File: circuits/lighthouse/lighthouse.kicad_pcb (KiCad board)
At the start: 2 copper layers, 84 x 112 mm, 83 parts, among them IC1 SX1308, J1 USB_C_Receptacle_PowerOnly_6P, J2 USB_B_Micro, Q1 S9013, Q2 FS8205A, Q3 2N7002K, Q4 SS8050, Q5 SS8050, U1 R300, U10 CP2102-GMR, U2 AMS1117-3.3, U4 TP4056-42-ESOP8, U5 DW01A, U6 AMS1117-3.3, U7 ESP32-WROOM-32

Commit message: Rewamped the pcb
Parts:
- removed J2: USB_B_Micro, Connector_USB:USB_Micro-B_Amphenol_10103594-0001LF_Horizontal
- removed R8: 2, Resistor_SMD:R_1206_3216Metric_Pad1.30x1.75mm_HandSolder
- BZ1: footprint Buzzer_Beeper:Buzzer_12x9.5RM7.6 -> Buzzer_Beeper:MagneticBuzzer_PUI_AT-0927-TT-6-R
- C4, C5: value C -> 10u
- J1: value USB_C_Receptacle_PowerOnly_6P -> USB_C_Receptacle_6P
- moved R4 28.4 mm to (91.4, 105.8)
- moved D12 25.6 mm to (82.7, 118.0)
- moved C6 21.4 mm to (112.3, 103.5)
- moved C7 21.4 mm to (112.3, 106.0)
- moved C12 21.3 mm to (88.0, 117.4), turned to -90 degrees
- moved Q1 20.9 mm to (97.0, 105.7)
- moved D8 20.9 mm to (104.3, 104.0), turned to -90 degrees
- moved R7 20.7 mm to (91.5, 103.0), turned to 180 degrees
- moved C13 20.5 mm to (88.0, 110.4), turned to 90 degrees
- moved R5 19.9 mm to (49.5, 110.0)
- moved BZ1 19.9 mm to (95.0, 118.0)
- moved R32 19.4 mm to (49.5, 94.8), turned to 90 degrees
- moved R16 19.3 mm to (107.3, 104.0), turned to 90 degrees
- moved D11 18.8 mm to (113.7, 114.9)
- moved R19 18.8 mm to (111.2, 114.9)
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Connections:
- net Net-(U7-IO22) renamed RFID_PW_SENSE
- C3 pad 1: Net-(U4-CE) -> +5V
- D5 pad 2: Net-(D5-A) -> +5V
- D6 pad 2: Net-(D5-A) -> +5V
- J1 pad A5: Net-(J1-CC1) -> /Charger/D+
- J1 pad A9: Net-(U4-CE) -> +5V
- J1 pad B5: Net-(J1-CC2) -> /Charger/D-
- J1 pad B9: Net-(U4-CE) -> +5V
- R32 pad 1: Net-(J1-CC2) -> /Charger/D-
- R33 pad 1: Net-(J1-CC1) -> /Charger/D+
- U10 pad 4: Net-(J2-D+) -> /Charger/D+
- U10 pad 5: Net-(J2-D-) -> /Charger/D-
- U4 pad 4: Net-(U4-CE) -> +5V
- U4 pad 8: Net-(U4-CE) -> +5V
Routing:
- net GND: track 167.3 -> 110.8 mm, vias 10 -> 14
- net Net-(U4-CE): track 42.8 -> 0.00 mm, vias 2 -> 0
- net +5V: track 119.8 -> 162.3 mm, vias 2 -> 4
- net RFID_PW: track 11.7 -> 44.1 mm
- net RFID_PW_SENSE: track 27.1 -> 46.7 mm
- net ESP25: track 53.1 -> 34.6 mm, vias 2 -> 4
- net /Charger/+BAT: track 90.7 -> 72.6 mm
- net +3.3V: track 127.7 -> 109.9 mm
- net EN: track 28.2 -> 11.0 mm
- net /Charger/-BAT: track 67.4 -> 81.5 mm
- net Net-(Q1-B): track 18.1 -> 4.57 mm
- net /Charger/D+: track 0.00 -> 11.9 mm
- net /Charger/D-: track 0.00 -> 11.0 mm
- net Net-(D5-A): track 10.2 -> 0.00 mm
- net Net-(U1-EN): track 13.1 -> 3.43 mm
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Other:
- board size 84 x 112 mm -> 83 x 80 mm

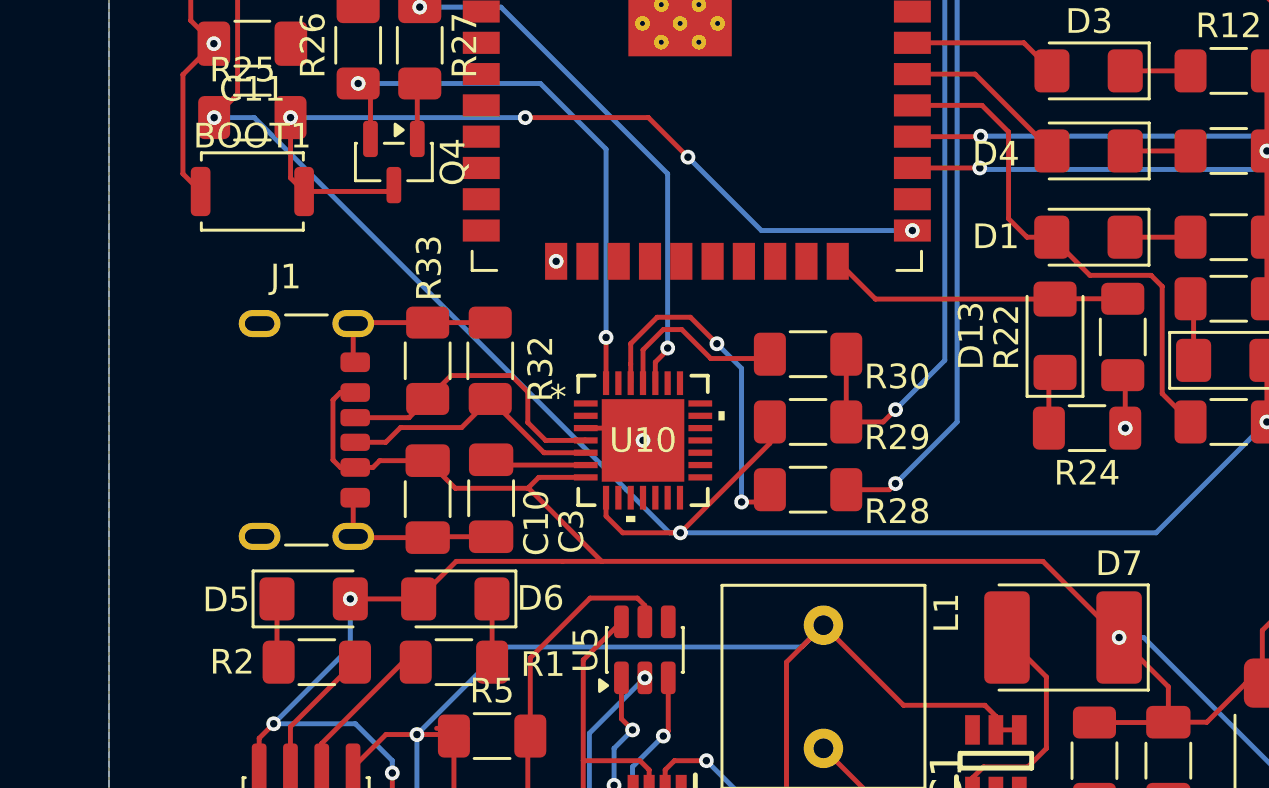
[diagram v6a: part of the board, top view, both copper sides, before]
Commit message: Changed to a correct usb C port
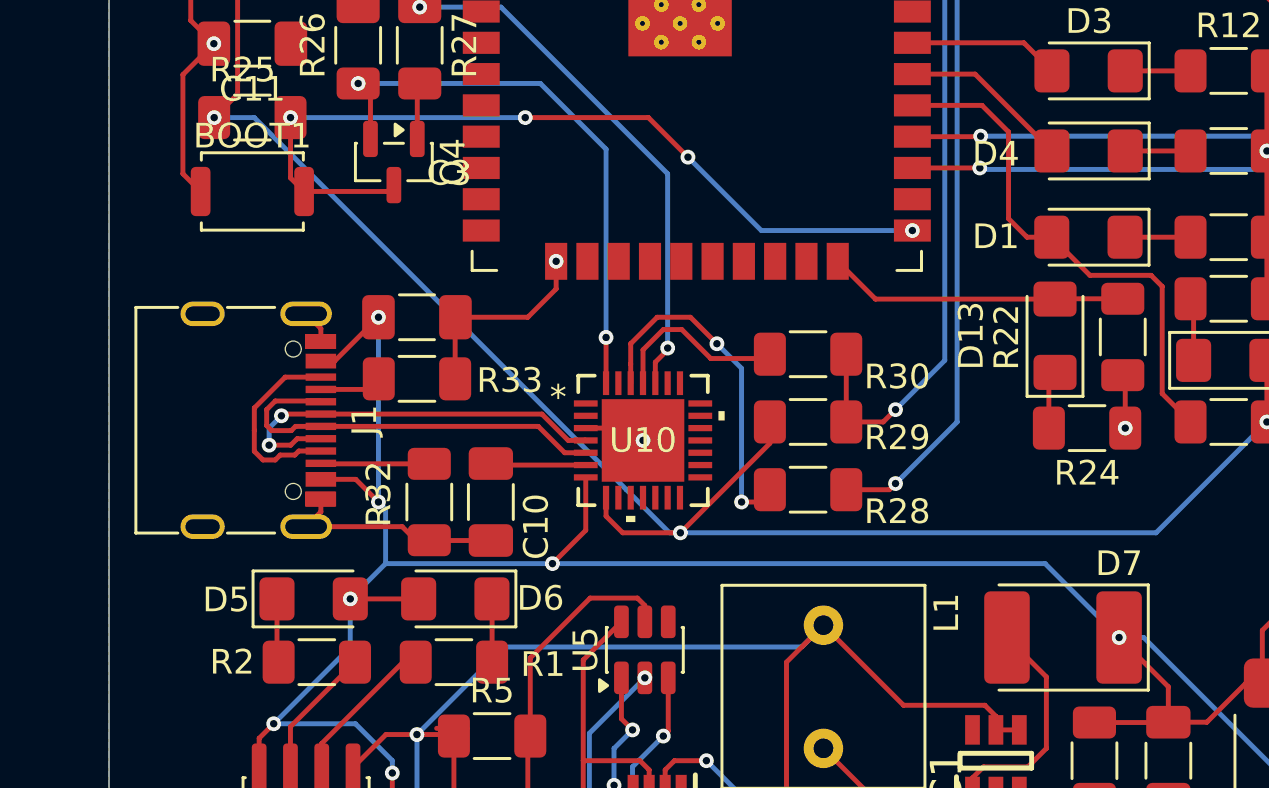
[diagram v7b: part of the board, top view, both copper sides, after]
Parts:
- J1: value USB_C_Receptacle_6P -> USB_C_Receptacle_USB2.0_14P; footprint Connector_USB:USB_C_Receptacle_GCT_USB4125-xx-x_6P_TopMnt_Horizontal -> Connector_USB:USB_C_Receptacle_G-Switch_GT-USB-7010ASV
- moved C3 7.40 mm to (46.5, 93.0), turned to 0 degrees
- moved R32 6.24 mm to (47.0, 100.5), turned to -90 degrees
- moved J1 2.08 mm to (38.9, 97.2)
- moved R33 0.85 mm to (46.5, 95.5), turned to 0 degrees
- moved C10 0.15 mm to (49.5, 100.5)
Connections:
- J1 pad A5: /Charger/D+ -> /Charger/CC1
- J1 pad B5: /Charger/D- -> /Charger/CC2
- R32 pad 1: /Charger/D- -> /Charger/CC2
- R33 pad 1: /Charger/D+ -> /Charger/CC1
- U10 pad 4: /Charger/D+ -> Net-(U10-D+)
- U10 pad 5: /Charger/D- -> Net-(U10-D-)
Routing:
- net Net-(U10-D-): track 0.00 -> 16.6 mm
- net Net-(U10-D+): track 0.00 -> 16.5 mm, vias 0 -> 2
- net /Charger/D+: track 11.9 -> 0.00 mm
- net /Charger/D-: track 11.0 -> 0.00 mm
- net (no net): track 0.00 -> 7.98 mm
- net /Charger/CC2: track 0.00 -> 4.41 mm
- net GND: track 110.8 -> 114.9 mm
- net +5V: track 162.3 -> 166.1 mm, vias 4 -> 7
- net /Charger/CC1: track 0.00 -> 2.53 mm

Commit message: Cleaned up schematics
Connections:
- Q2 pad 5: Net-(Q2-G2) -> GND
- R5 pad 1: /Charger/+BAT -> Net-(U5-VCC)
- R5 pad 2: Net-(U5-VCC) -> /Charger/+BAT
- R6 pad 1: GND -> Net-(U5-CS)
- R6 pad 2: Net-(U5-CS) -> GND
- U5 pad 3: Net-(Q2-G2) -> GND
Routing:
- net GND: track 114.9 -> 127.6 mm, vias 14 -> 16
- net Net-(Q2-G2): track 12.8 -> 0.00 mm, vias 2 -> 0
- net /R300/GND: track 52.3 -> 56.5 mm
- net Net-(D8-K): track 0.00 -> 3.00 mm
